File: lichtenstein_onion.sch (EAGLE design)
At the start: 13 parts, among them J1 MAGJACK, U1 ONION-OMEGA2

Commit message: Added 3V3 and 1V8 voltage regulators
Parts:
- added C10, C13, C7: 47µF, rcl:CPOL-EUCT6032
- added C11, C12, C6: 100nF, rcl:C-EUC0805
- added C8: 3.3nF, rcl:C-EUC0805
- added C9: 100µF, rcl:CPOL-EUSMCD
- added IC1: TPS706-1V8, lichtenstein_onion:TPS706SOT23-5
- added IC2: LM2852Y-3V3, lichtenstein_onion:LM2852HTSSOP14
- added L1: 18µH, lichtenstein_onion:SRR1050A
- C2: device rcl:CPOL-EU150CLZ-1014 -> rcl:CPOL-EUCT6032; MOUSER (none) -> 581-NOSD107M006
- R5, R6: value 330R -> 680R
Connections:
- new net N$7: IC2.SW, L1.1
- new net N$8: C8.2, IC2.SS
- new net V+: C10.+, C11.1, IC2.AVIN, IC2.EN, IC2.PVIN
- new net VCORE: C6.1, C7.+, IC1.VOUT
- net +3V3: now also C12.1, C13.+, C9.+, IC1.VIN, IC2.SNS, L1.2
- net GND: now also C10.-, C11.2, C12.2, C13.-, C6.2, C7.-, C8.1, C9.-, IC1.GND, IC2.PGND, IC2.SGND

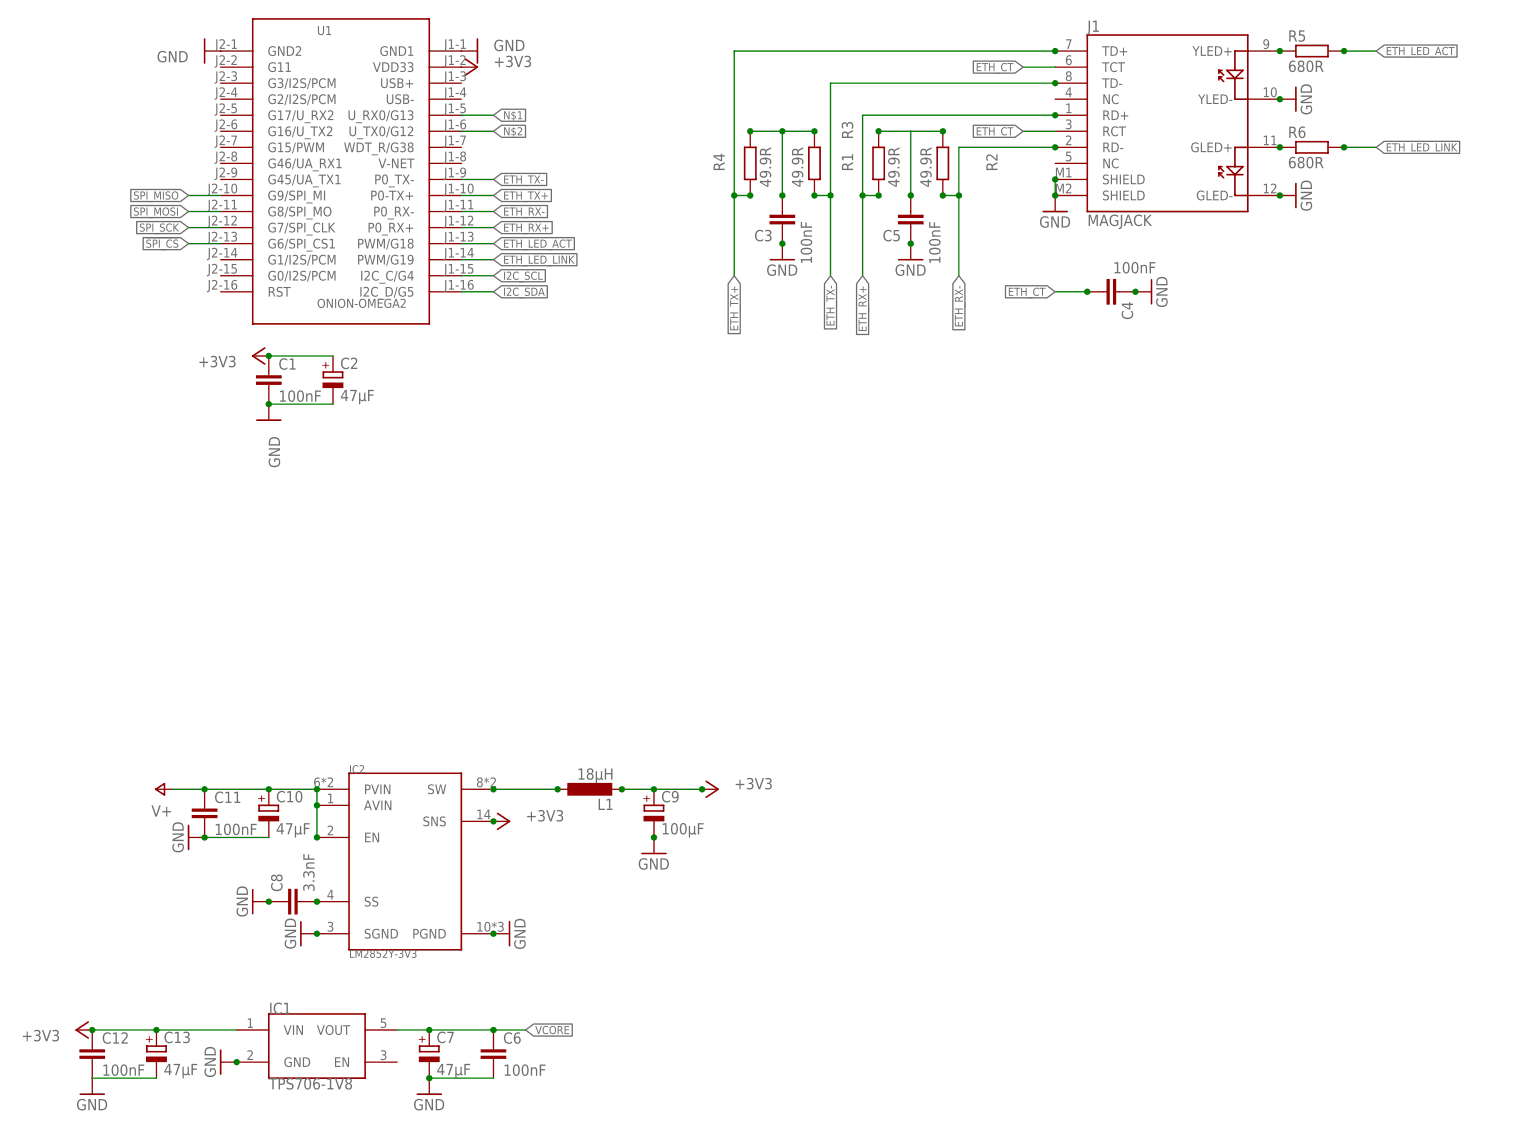
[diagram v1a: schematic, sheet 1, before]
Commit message: Added CPLD, output drivers, IO expanders
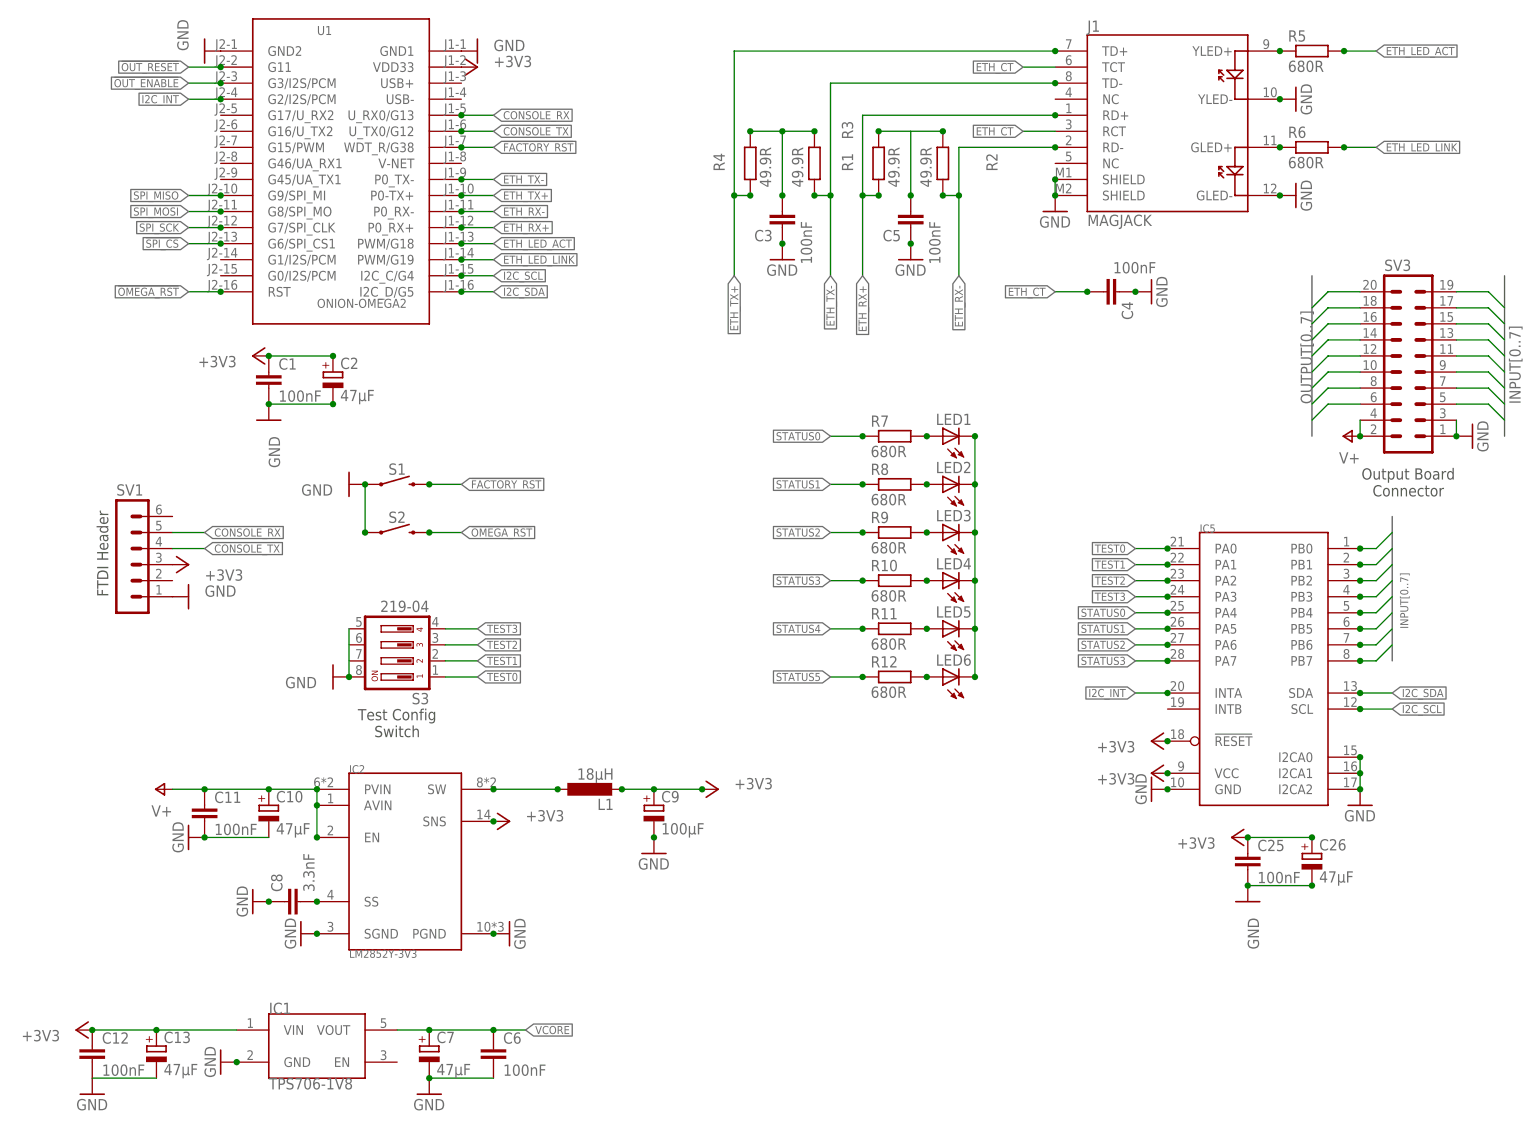
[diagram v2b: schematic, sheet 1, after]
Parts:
- added C14, C16, C17, C18, C20, C21, C23, C24, C25: 100nF, rcl:C-EUC0805
- added C15, C19, C22, C26: 47µF, rcl:CPOL-EUCT6032
- added IC3: 5M160ZE64, lichtenstein_onion:5M160ZE64
- added IC4: (no value), lichtenstein_onion:TXB0108TSSOP20
- added IC5: (no value), lichtenstein_onion:MCP23017SSOP28
- added LED1, LED2, LED3, LED4, LED5, LED6: (no value), led:LEDCHIPLED_1206
- added R10, R11, R12, R7, R8, R9: 680R, rcl:R-EU_M0805
- added S1, S2: MOMENTARY-SWITCH-SPST-PTH-6.0MM, SparkFun-Switches:MOMENTARY-SWITCH-SPST-PTH-6.0MM
- added S3: 219-04, switch-dil:219-04
- added SV1: (no value), con-lstb:MA06-1
- added SV2: (no value), con-lstb:MA05-2
- added SV3: (no value), con-lstb:MA10-2
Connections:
- new net !FACTORY_RST: S1.2, U1.WDT_R/G38
- new net !OMEGA_RST: S2.2, U1.RST
- new net !OUT_ENABLE: IC3.IO2, U1.G3/I2S/PCM
- new net !OUT_RESET: IC3.IO1, U1.G11
- new net BUFFER_OE: IC3.IO46, IC4.OE
- new net CONSOLE_RX: SV1.5, U1.U_RX0/G13
- new net CONSOLE_TX: SV1.4, U1.U_TX0/G12
- new net CPLD_TCK: IC3.TCK, SV2.1
- new net CPLD_TDI: IC3.TDI, SV2.9
- new net CPLD_TDO: IC3.TDO, SV2.3
- new net CPLD_TMS: IC3.TMS, SV2.5
- new net I2C_INT: IC5.INTA, U1.G2/I2S/PCM
- new net INPUT0: IC5.PB0, SV3.5
- new net INPUT1: IC5.PB1, SV3.7
- new net INPUT2: IC5.PB2, SV3.9
- new net INPUT3: IC5.PB3, SV3.11
- new net INPUT4: IC5.PB4, SV3.13
- new net INPUT5: IC5.PB5, SV3.15
- new net INPUT6: IC5.PB6, SV3.17
- new net INPUT7: IC5.PB7, SV3.19
- new net N$10: LED3.A, R9.2
- new net N$11: LED4.A, R10.2
- new net N$12: LED5.C, LED6.C
- new net N$13: LED5.A, R11.2
- new net N$14: LED6.A, R12.2
- new net N$9: LED2.A, R8.2
- new net OUTPUT0: IC4.B1, SV3.6
- new net OUTPUT1: IC4.B2, SV3.8
- new net OUTPUT2: IC4.B3, SV3.10
- new net OUTPUT3: IC4.B4, SV3.12
- new net OUTPUT4: IC4.B5, SV3.14
- new net OUTPUT5: IC4.B6, SV3.16
- new net OUTPUT6: IC4.B7, SV3.18
- new net OUTPUT7: IC4.B8, SV3.20
- new net OUT_3V0: IC3.IO34, IC4.A1
- new net OUT_3V1: IC3.IO35, IC4.A2
- new net OUT_3V2: IC3.IO36, IC4.A3
- new net OUT_3V3: IC3.IO37, IC4.A4
- new net OUT_3V4: IC3.IO38, IC4.A5
- new net OUT_3V5: IC3.IO43, IC4.A6
- new net OUT_3V6: IC3.IO44, IC4.A7
- new net OUT_3V7: IC3.IO45, IC4.A8
- new net STATUS0: IC5.PA4, R7.1
- new net STATUS1: IC5.PA5, R8.1
- new net STATUS2: IC5.PA6, R9.1
- new net STATUS3: IC5.PA7, R10.1
- new net STATUS4: IC3.IO11, R11.1
- new net STATUS5: IC3.IO12, R12.1
- new net TEST0: IC5.PA0, S3.1
- new net TEST1: IC5.PA1, S3.2
- new net TEST2: IC5.PA2, S3.3
- new net TEST3: IC5.PA3, S3.4
- net !SPI_CS: now also IC3.IO3
- net +3V3: now also C14.1, C15.+, C16.1, C17.1, C18.1, C19.+, C23.1, C25.1, C26.+, IC3.VCCIO1, IC3.VCCIO2, IC4.VCCA, IC5.!RESET, IC5.VCC, SV1.3, SV2.4
- net GND: now also C14.2, C15.-, C16.2, C17.2, C18.2, C19.-, C20.2, C21.2, C22.-, C23.2, C24.2, C25.2, C26.-, IC3.GND, IC4.GND, IC5.GND, IC5.I2CA0, IC5.I2CA1, IC5.I2CA2, S1.1, S2.1, S3.5, S3.8, SV1.1, SV2.10, SV2.2, SV3.1, SV3.3
- net I2C_SCL: now also IC5.SCL
- net I2C_SDA: now also IC5.SDA
- net N$1: now also LED1.C, LED2.C, LED3.C, LED4.C; no longer U1.U_RX0/G13
- net N$2: now also LED1.A, R7.2; no longer U1.U_TX0/G12
- net SPI_MISO: now also IC3.IO4
- net SPI_MOSI: now also IC3.IO5
- net SPI_SCK: now also IC3.CLK1, IC3.IO10
- net V+: now also C24.1, IC4.VCCB, SV3.2, SV3.4
- net VCORE: now also C20.1, C21.1, C22.+, IC3.VCCINT
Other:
- note added: "CPLD Programming Header"
- note added: "FTDI Header"
- note added: "Output Board Connector"
- note added: "Test Config Switch"
